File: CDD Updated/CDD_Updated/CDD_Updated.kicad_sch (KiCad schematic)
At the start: 5 parts, among them U1 DPS368XTSA1_PRESSURE_SENSOR, U2 MAX30101, U3 MOUDLE-SEEEDUINO-XIAO-ESP32C3

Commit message: update files
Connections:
- net GND: now also U1.1 (GND), U1.7 (GND__1), U2.5 (GND), U3.13 (GND)
- net at U3.1 (PA02_A0_D0): no longer U1.3 (SDI)
- net 3V3: now reaches C1.1, C2.1, U1.6 (VDDIO), U1.8 (VDD), U2.4 (3V3), U3.12 (3V3)
- net RST: now reaches U2.1 (RST), U3.2 (PA4_A1_D1)
- net MFIO: now reaches U2.6 (MFIO), U3.3 (PA10_A2_D2)
- net SDA: now reaches U2.3 (SDA), U3.5 (PA8_A4_D4_SDA)
- net SDA: now also U1.3 (SDI)
- net SCK: now reaches U2.2 (SCL), U3.6 (PA9_A5_D5_SCL)
- net SCK: now also U1.4 (SCK)
- no-connect marks 10 -> 9

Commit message: Updated footprints and PCB
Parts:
- added BT1: Battery_Cell, symbol Device:Battery_Cell
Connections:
- net VDD: no longer names the net of U3.15 (BAT_+)
- net VDD: now also BT1.1 (+)
- net VSS: no longer names the net of U3.16 (BAT_-)
- net VSS: now also BT1.2 (-)
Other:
- moved on the sheet: C1, C2

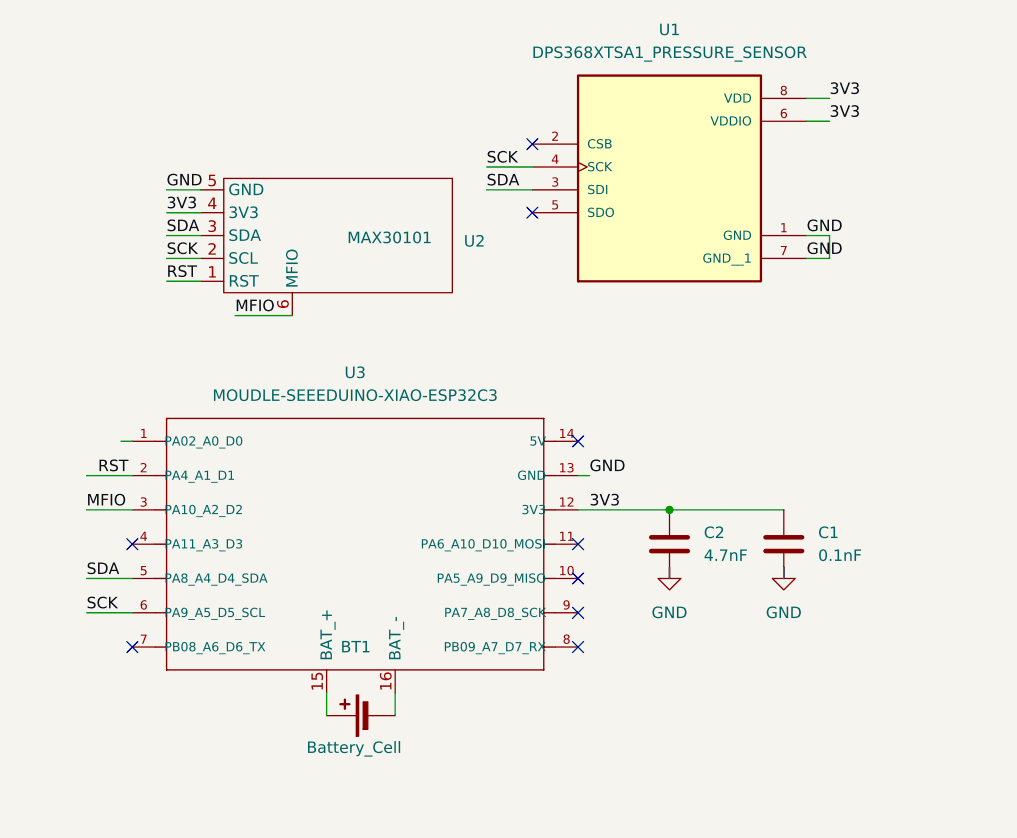
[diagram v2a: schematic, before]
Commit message: Update KiCAD files and route PCB
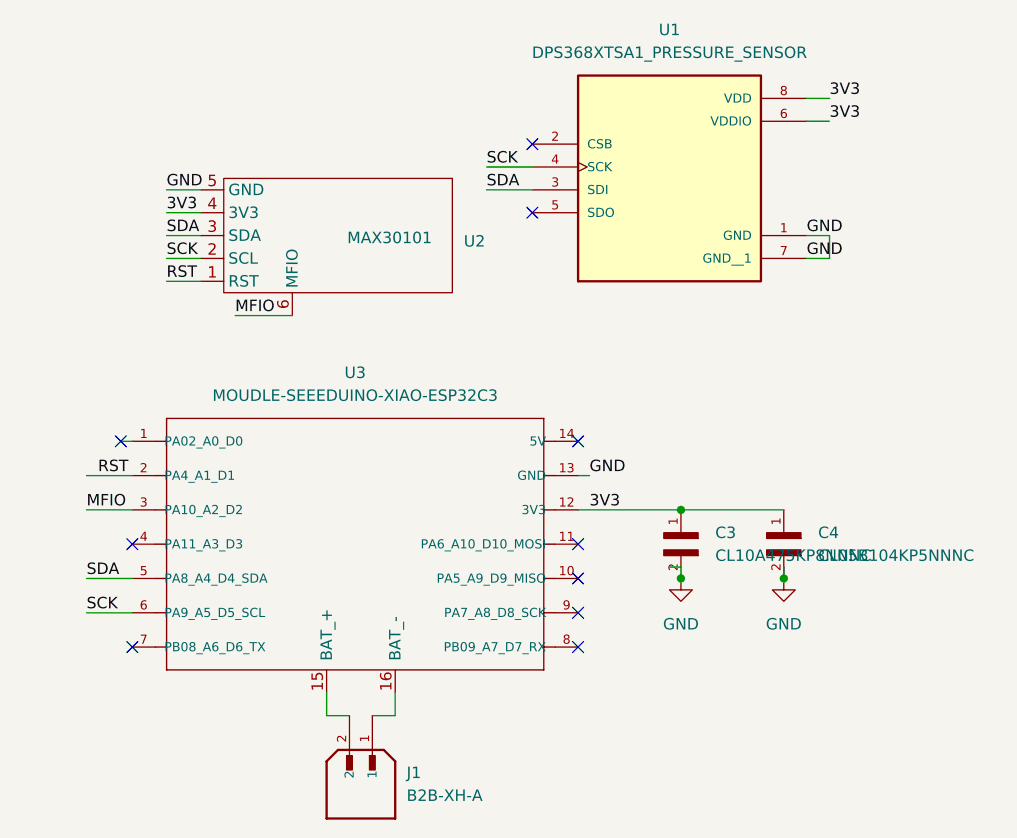
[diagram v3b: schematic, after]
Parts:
- removed BT1: Battery_Cell, symbol Device:Battery_Cell
- removed C1: 0.1nF, symbol Device:C
- removed C2: 4.7nF, symbol Device:C
- added C3: CL10A475KP8NNNC, CDD Updated:CAPC1608X90N_47uF, symbol CDD_Library_Updated:CL10A475KP8NNNC
- added C4: CL05B104KP5NNNC, CDD Updated:CAPC1005X55N_0.1NF, symbol CDD_Library_Updated:CL05B104KP5NNNC
- added J1: B2B-XH-A, CDD Updated:JST_B2B-XH-A, symbol CDD_Library_Updated:B2B-XH-A
- U1: footprint DPS368XTSA1:XDCR_DPS368XTSA1 -> CDD Updated:XDCR_DPS368XTSA1_Pressure_Sensor
- U2: footprint (none) -> CDD Updated:MAX30101_PPG_Sensor
- U3: footprint MOUDLE14P-SMD-2.54-21X17.8MM -> CDD Updated:MOUDLE14P-SMD-2.54-21X17.8MM
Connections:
- net 3V3: now also C3.1, C4.1
- net GND: now also C3.2, C4.2
- net at U3.15 (BAT_+): now also J1.2
- net at U3.16 (BAT_-): now also J1.1
- no-connect marks 9 -> 10

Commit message: update pcb and schematic - remove extra sensors
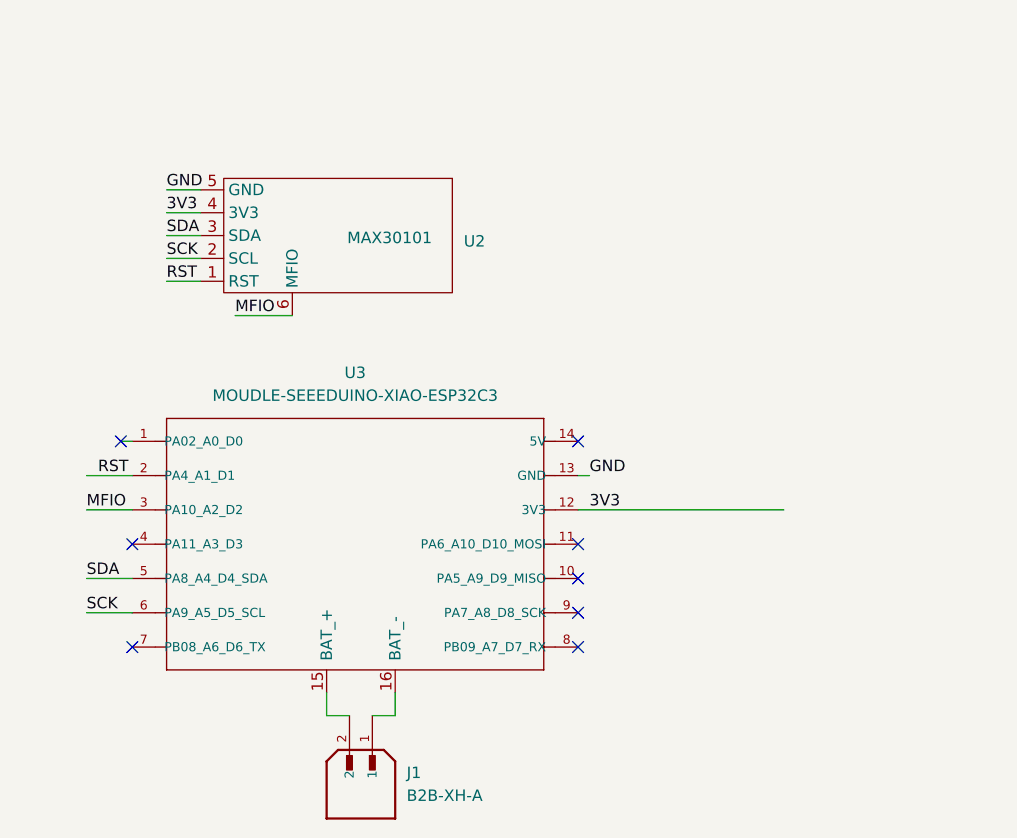
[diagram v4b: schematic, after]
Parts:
- removed C3: CL10A475KP8NNNC, CDD Updated:CAPC1608X90N_47uF, symbol CDD_Library_Updated:CL10A475KP8NNNC
- removed C4: CL05B104KP5NNNC, CDD Updated:CAPC1005X55N_0.1NF, symbol CDD_Library_Updated:CL05B104KP5NNNC
- removed U1: DPS368XTSA1_PRESSURE_SENSOR, CDD Updated:XDCR_DPS368XTSA1_Pressure_Sensor, symbol CDD_Library_Updated:DPS368XTSA1
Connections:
- no-connect marks 10 -> 8
